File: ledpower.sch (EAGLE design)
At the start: 40 parts, among them IC1 74HCT595D, SW1 EC12E_SW, SW2 EC12E_SW, U1 LCD-16X2NOHOLES, X1 5566-24

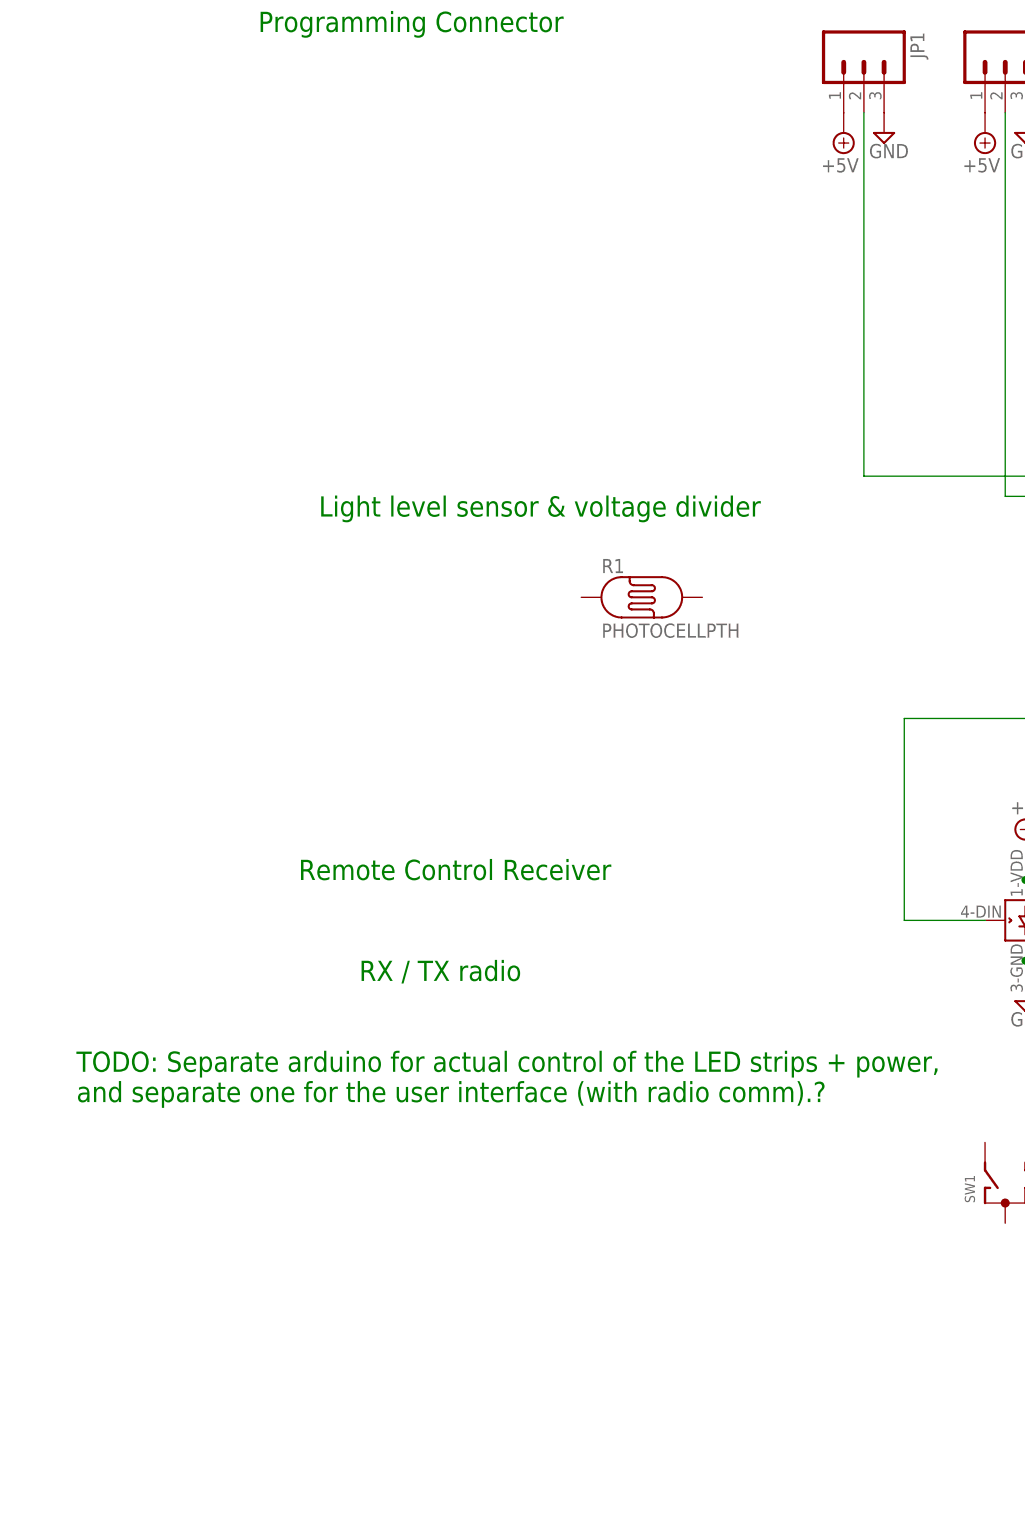
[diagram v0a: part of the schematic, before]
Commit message: Added todo comments.
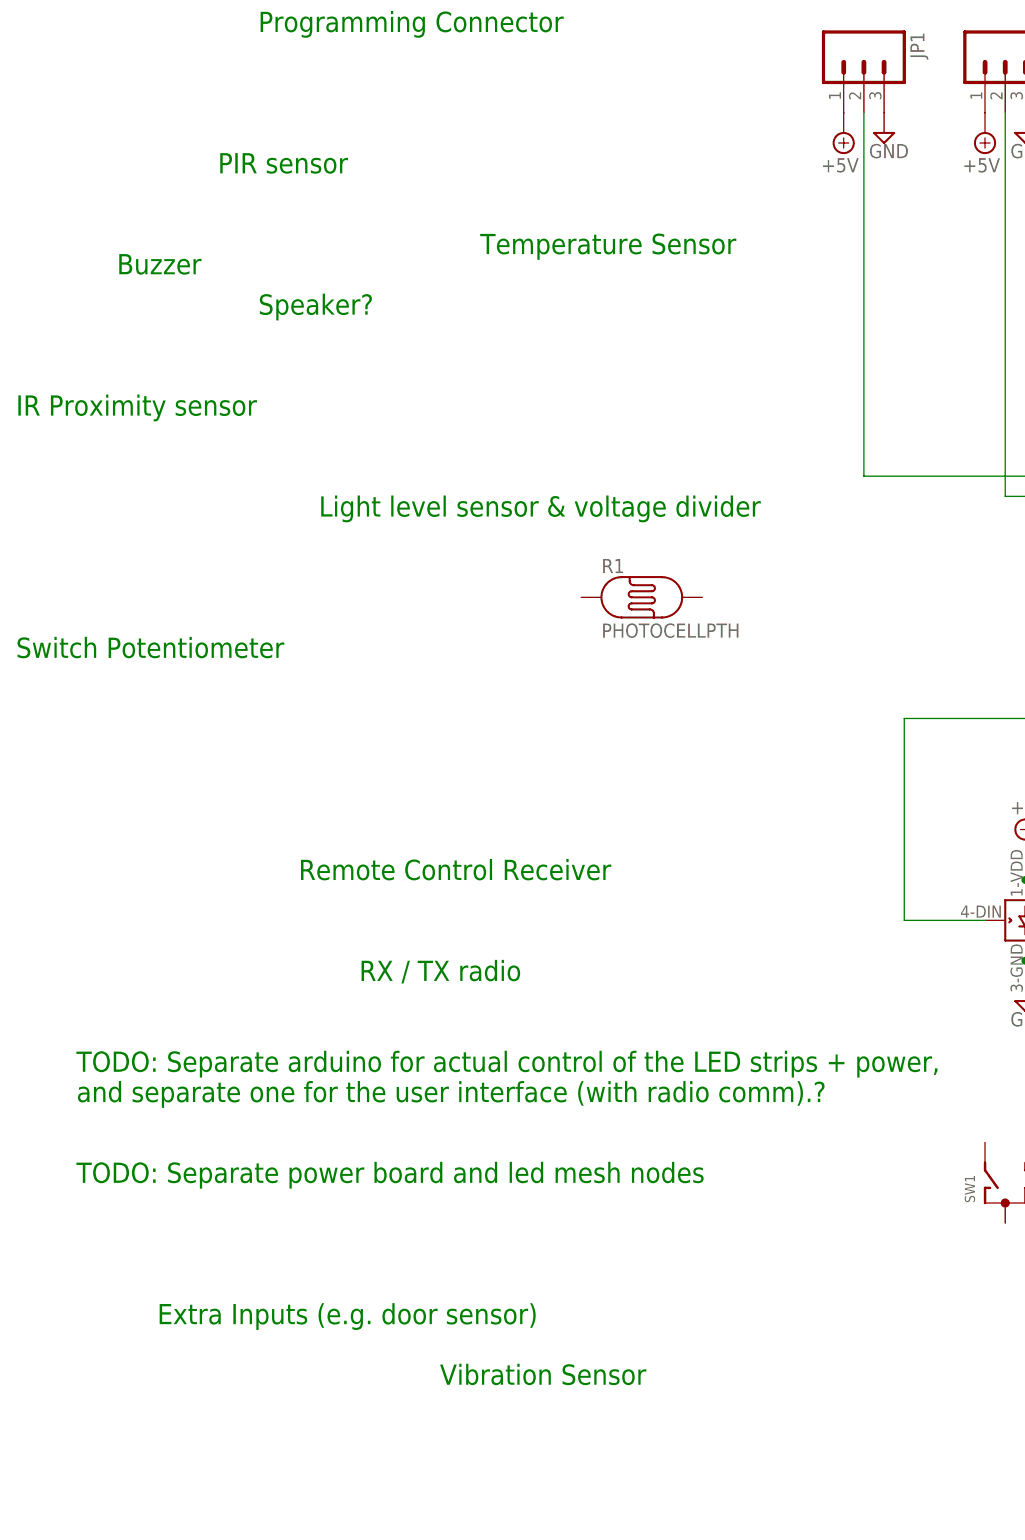
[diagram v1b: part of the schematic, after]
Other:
- note added: "Buzzer"
- note added: "Extra Inputs (e.g. door sensor)"
- note added: "IR Proximity sensor"
- note added: "PIR sensor"
- note added: "Speaker?"
- note added: "Switch Potentiometer"
- note added: "TODO: Separate power board and led mesh nodes"
- note added: "Temperature Sensor"
- note added: "Vibration Sensor"
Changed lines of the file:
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@@
 <text x="-124.46" y="-7.62" size="2.54" layer="91">TODO: Separate arduino for actual control of the LED strips + power,
 and separate one for the user interface (with radio comm).?</text>
+<text x="-124.46" y="-17.78" size="2.54" layer="91">TODO: Separate power board and led mesh nodes</text>
+<text x="-106.68" y="109.22" size="2.54" layer="91">PIR sensor</text>
+<text x="-119.38" y="96.52" size="2.54" layer="91">Buzzer</text>
+<text x="-101.6" y="91.44" size="2.54" layer="91">Speaker?</text>
+<text x="-132.08" y="78.74" size="2.54" layer="91">IR Proximity sensor</text>
+<text x="-132.08" y="48.26" size="2.54" layer="91">Switch Potentiometer</text>
+<text x="-114.3" y="-35.56" size="2.54" layer="91">Extra Inputs (e.g. door sensor)</text>
+<text x="-78.74" y="-43.18" size="2.54" layer="91">Vibration Sensor</text>
+<text x="-73.66" y="99.06" size="2.54" layer="91">Temperature Sensor</text>
 </plain>
 <instances>
